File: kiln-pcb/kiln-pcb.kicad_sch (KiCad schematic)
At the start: 12 parts, among them J1 TFT, J2 TEMP, J3 ROTARY, J4 Relay, U1 WeMos_D1_mini

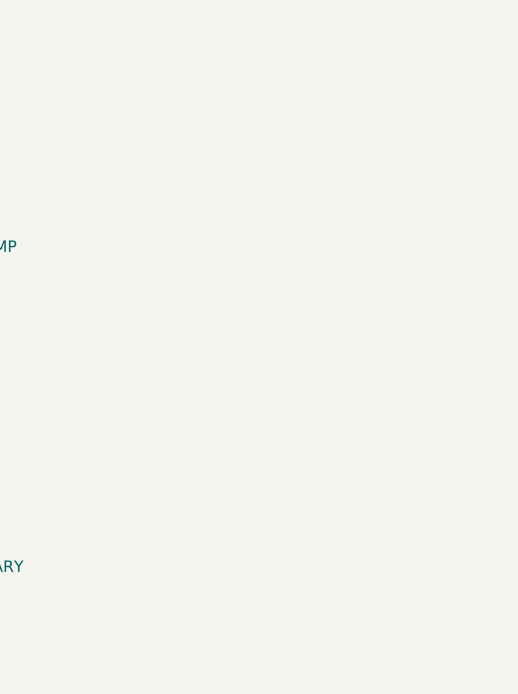
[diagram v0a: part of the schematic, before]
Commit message: Added simple PID for relay
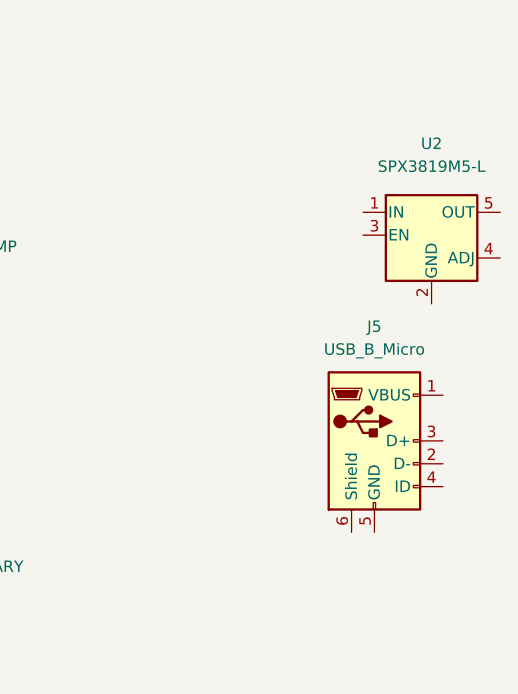
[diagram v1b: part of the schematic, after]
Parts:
- added J5: USB_B_Micro, symbol Connector:USB_B_Micro
- added U2: SPX3819M5-L, Package_TO_SOT_SMD:SOT-23-5, symbol Regulator_Linear:SPX3819M5-L
- H1, H2, H3, H4: footprint MountingHole:MountingHole_3.2mm_M3 -> MountingHole:MountingHole_3.2mm_M3_Pad_Via
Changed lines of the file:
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@@
       (effects (font (size 1.27 1.27)) (justify left))
     )
-    (property "Footprint" "MountingHole:MountingHole_3.2mm_M3" (id 2) (at 134.62 125.73 0)
+    (property "Footprint" "MountingHole:MountingHole_3.2mm_M3_Pad_Via" (id 2) (at 134.62 125.73 0)
       (effects (font (size 1.27 1.27)) hide)
     )
@@
     (pin "1")
   )
+  (symbol (lib_id "Regulator_Linear:SPX3819M5-L") (at 205.74 44.45 0) (unit 1)
+    (in_bom yes) (on_board yes) (fields_autoplaced)
+    (property "Reference" "U2" (id 0) (at 205.74 34.29 0))
+    (property "Value" "SPX3819M5-L" (id 1) (at 205.74 36.83 0))
+    (property "Footprint" "Package_TO_SOT_SMD:SOT-23-5" (id 2) (at 205.74 36.195 0)
+      (effects (font (size 1.27 1.27)) hide)
+    )
+    (property "Datasheet" "https://www.exar.com/content/document.ashx?id=22106&languageid=1033&type=Datasheet&partnumber=SPX3819&filename=SPX3819.pdf&part=SPX3819" (id 3) (at 205.74 44.45 0)
+      (effects (font (size 1.27 1.27)) hide)
+    )
+    (pin "1")
+    (pin "2")
+    (pin "3")
+    (pin "4")
+    (pin "5")
+  )
   (symbol (lib_id "Connector:TestPoint") (at 63.5 99.06 270) (unit 1)
     (in_bom yes) (on_board yes) (fields_autoplaced)
@@
       (effects (font (size 1.27 1.27)) (justify left))
     )
-    (property "Footprint" "MountingHole:MountingHole_3.2mm_M3" (id 2) (at 124.46 115.57 0)
+    (property "Footprint" "MountingHole:MountingHole_3.2mm_M3_Pad_Via" (id 2) (at 124.46 115.57 0)
       (effects (font (size 1.27 1.27)) hide)
     )
@@
       (effects (font (size 1.27 1.27)) (justify left))
     )
-    (property "Footprint" "MountingHole:MountingHole_3.2mm_M3" (id 2) (at 124.46 125.73 0)
+    (property "Footprint" "MountingHole:MountingHole_3.2mm_M3_Pad_Via" (id 2) (at 124.46 125.73 0)
       (effects (font (size 1.27 1.27)) hide)
     )
@@
       (effects (font (size 1.27 1.27)) (justify left))
     )
-    (property "Footprint" "MountingHole:MountingHole_3.2mm_M3" (id 2) (at 133.35 115.57 0)
+    (property "Footprint" "MountingHole:MountingHole_3.2mm_M3_Pad_Via" (id 2) (at 133.35 115.57 0)
       (effects (font (size 1.27 1.27)) hide)
     )
@@
     (pin "4")
     (pin "5")
+  )
+  (symbol (lib_id "Connector:USB_B_Micro") (at 199.39 67.31 0) (unit 1)
+    (in_bom yes) (on_board yes) (fields_autoplaced)
+    (property "Reference" "J5" (id 0) (at 199.39 54.61 0))
+    (property "Value" "USB_B_Micro" (id 1) (at 199.39 57.15 0))
+    (property "Footprint" "" (id 2) (at 203.2 68.58 0)
+      (effects (font (size 1.27 1.27)) hide)
+    )
+    (property "Datasheet" "~" (id 3) (at 203.2 68.58 0)
+      (effects (font (size 1.27 1.27)) hide)
+    )
+    (pin "1")
+    (pin "2")
+    (pin "3")
+    (pin "4")
+    (pin "5")
+    (pin "6")
   )
   (sheet_instances
@@
     )
     (path "/aa1c6f47-cbd4-4cbd-8265-e5ac08b7ffc8"
-      (reference "H1") (unit 1) (value "MountingHole") (footprint "MountingHole:MountingHole_3.2mm_M3")
+      (reference "H1") (unit 1) (value "MountingHole") (footprint "MountingHole:MountingHole_3.2mm_M3_Pad_Via")
     )
     (path "/b2944857-047d-4655-a00b-49e658220448"
-      (reference "H2") (unit 1) (value "MountingHole") (footprint "MountingHole:MountingHole_3.2mm_M3")
+      (reference "H2") (unit 1) (value "MountingHole") (footprint "MountingHole:MountingHole_3.2mm_M3_Pad_Via")
     )
     (path "/d068a394-7054-45f9-ac53-014bf75c7213"
-      (reference "H3") (unit 1) (value "MountingHole") (footprint "MountingHole:MountingHole_3.2mm_M3")
+      (reference "H3") (unit 1) (value "MountingHole") (footprint "MountingHole:MountingHole_3.2mm_M3_Pad_Via")
     )
     (path "/25f1074a-6ae7-40ed-8106-5e5622cabe99"
-      (reference "H4") (unit 1) (value "MountingHole") (footprint "MountingHole:MountingHole_3.2mm_M3")
+      (reference "H4") (unit 1) (value "MountingHole") (footprint "MountingHole:MountingHole_3.2mm_M3_Pad_Via")
     )
     (path "/5fada503-749c-4ab1-b15f-4f7e43d6c0e6"
@@
       (reference "J4") (unit 1) (value "Relay") (footprint "Connector_PinHeader_2.54mm:PinHeader_1x03_P2.54mm_Vertical")
     )
+    (path "/e37d567c-6591-4d58-92e7-b351e9f98d1e"
+      (reference "J5") (unit 1) (value "USB_B_Micro") (footprint "Connector_USB:USB_Micro-B_Molex-105017-0001")
+    )
     (path "/4bb6aa50-20a8-40c0-9694-aa4503d2e061"
       (reference "TP1") (unit 1) (value "5V test") (footprint "TestPoint:TestPoint_Pad_D2.0mm")
@@
       (reference "U1") (unit 1) (value "WeMos_D1_mini") (footprint "Module:WEMOS_D1_mini_light")
     )
-  )
+    (path "/87e2c0d2-6681-45e0-8731-ac0b4ab5761c"
+      (reference "U2") (unit 1) (value "SPX3819M5-L") (footprint "Package_TO_SOT_SMD:SOT-23-5")
+    )
+  )

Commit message: PCB v1.1
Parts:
- removed J5: USB_B_Micro, symbol Connector:USB_B_Micro
- removed U2: SPX3819M5-L, Package_TO_SOT_SMD:SOT-23-5, symbol Regulator_Linear:SPX3819M5-L
- added J5, J6: Relay, Connector_PinHeader_2.54mm:PinHeader_1x03_P2.54mm_Vertical, symbol Connector:Conn_01x03_Male
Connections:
- net CS_T: now also U1.16 (TX); no longer J1.2 (Pin_2), U1.7 (CS/D8)
- net GND: now also J5.2 (Pin_2), J6.2 (Pin_2)
- net Sig_relay: now also J5.1 (Pin_1), J6.1 (Pin_1)
- net Vcc_relay: now also J5.3 (Pin_3), J6.3 (Pin_3)
- new net CS_TFT: J1.2 (Pin_2), U1.7 (CS/D8)
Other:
- moved on the sheet: J1, J2, J3, J4

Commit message: Basic README update
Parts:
- removed H1, H2, H3, H4: MountingHole, MountingHole:MountingHole_3.2mm_M3_Pad_Via, symbol Mechanical:MountingHole
- TP1: value 5V test -> 5V
- TP2: value GND test -> GND
- TP3: value Relay signal -> Relay
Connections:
- net Vcc_relay renamed 3V3
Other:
- moved on the sheet: J1, J2, J3, J4, J5, J6, TP1, TP2, TP3, U1

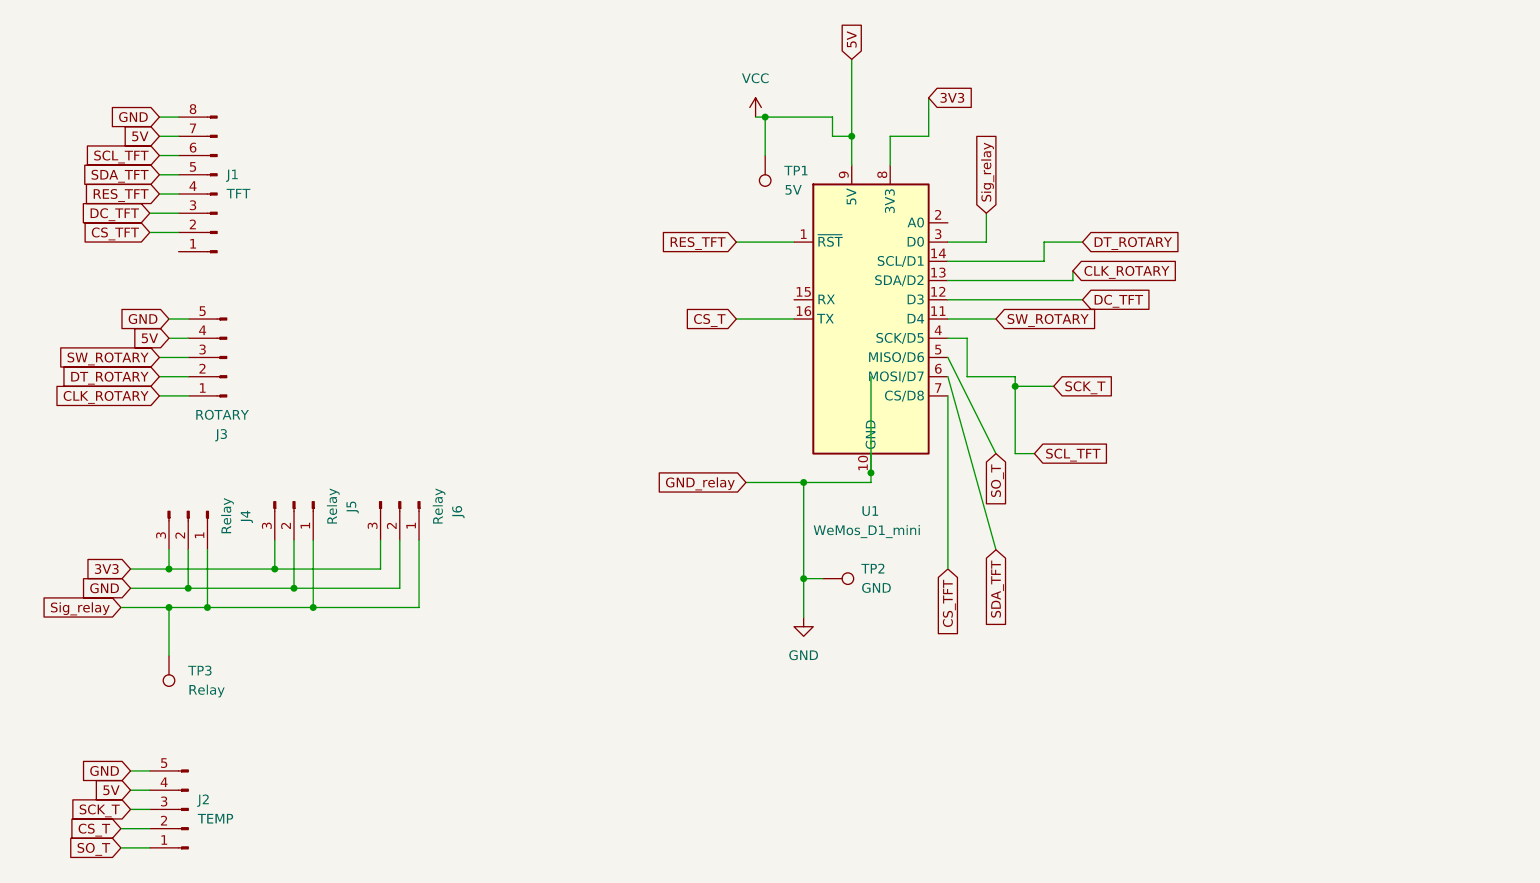
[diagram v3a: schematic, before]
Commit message: Added magnetic switch interrupt
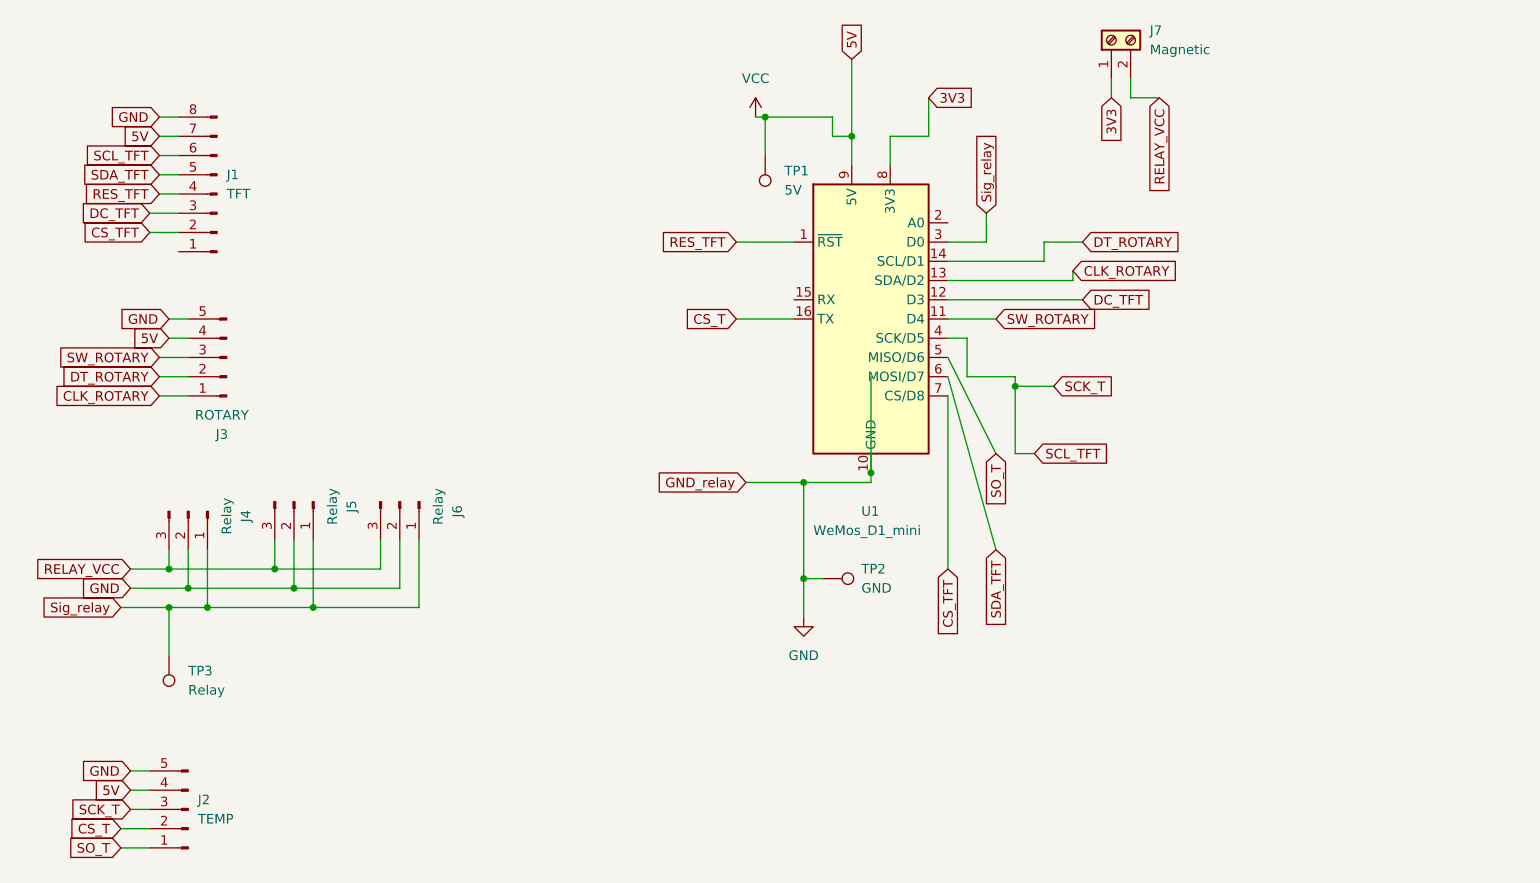
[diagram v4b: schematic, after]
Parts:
- added J7: Magnetic, TerminalBlock:TerminalBlock_bornier-2_P5.08mm, symbol Connector:Screw_Terminal_01x02
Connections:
- net 3V3: now also J7.1 (Pin_1); no longer J4.3 (Pin_3), J5.3 (Pin_3), J6.3 (Pin_3)
- new net RELAY_VCC: J4.3 (Pin_3), J5.3 (Pin_3), J6.3 (Pin_3), J7.2 (Pin_2)
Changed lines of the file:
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@@
+    (stroke (width 0) (type default) (color 0 0 0 0))
+  )
+  (wire (pts (xy 161.29 26.67) (xy 165.1 26.67))
     (stroke (width 0) (type default) (color 0 0 0 0))
   )
@@
     (stroke (width 0) (type default) (color 0 0 0 0))
   )
+  (wire (pts (xy 158.75 24.13) (xy 158.75 26.67))
+    (stroke (width 0) (type default) (color 0 0 0 0))
+  )
   (wire (pts (xy 50.8 85.09) (xy 50.8 91.44))
     (stroke (width 0) (type default) (color 0 0 0 0))
@@
     (stroke (width 0) (type default) (color 0 0 0 0))
   )
+  (wire (pts (xy 161.29 24.13) (xy 161.29 26.67))
+    (stroke (width 0) (type default) (color 0 0 0 0))
+  )
   (wire (pts (xy 137.16 66.04) (xy 137.16 88.9))
     (stroke (width 0) (type default) (color 0 0 0 0))
@@
     (stroke (width 0) (type default) (color 0 0 0 0))
   )
+  (global_label "3V3" (shape input) (at 158.75 26.67 270) (fields_autoplaced)
+    (effects (font (size 1.27 1.27)) (justify right))
+    (property "Intersheet References" "${INTERSHEET_REFS}" (id 0) (at 158.6706 32.5907 90)
+      (effects (font (size 1.27 1.27)) (justify right) hide)
+    )
+  )
   (global_label "5V" (shape input) (at 124.46 21.59 90) (fields_autoplaced)
     (effects (font (size 1.27 1.27)) (justify left))
@@
     )
   )
+  (global_label "RELAY_VCC" (shape input) (at 165.1 26.67 270) (fields_autoplaced)
+    (effects (font (size 1.27 1.27)) (justify right))
+    (property "Intersheet References" "${INTERSHEET_REFS}" (id 0) (at 165.0206 39.3036 90)
+      (effects (font (size 1.27 1.27)) (justify right) hide)
+    )
+  )
   (global_label "DT_ROTARY" (shape input) (at 154.94 45.72 0) (fields_autoplaced)
     (effects (font (size 1.27 1.27)) (justify left))
@@
     )
   )
-  (global_label "3V3" (shape input) (at 29.21 88.9 180) (fields_autoplaced)
-    (effects (font (size 1.27 1.27)) (justify right))
-    (property "Intersheet References" "${INTERSHEET_REFS}" (id 0) (at 23.2893 88.8206 0)
+  (global_label "RELAY_VCC" (shape input) (at 29.21 88.9 180) (fields_autoplaced)
+    (effects (font (size 1.27 1.27)) (justify right))
+    (property "Intersheet References" "${INTERSHEET_REFS}" (id 0) (at 16.5764 88.8206 0)
       (effects (font (size 1.27 1.27)) (justify right) hide)
     )
@@
     )
     (pin "1")
+  )
+  (symbol (lib_id "Connector:Screw_Terminal_01x02") (at 158.75 19.05 90) (unit 1)
+    (in_bom yes) (on_board yes) (fields_autoplaced)
+    (property "Reference" "J7" (id 0) (at 163.83 17.7799 90)
+      (effects (font (size 1.27 1.27)) (justify right))
+    )
+    (property "Value" "Magnetic" (id 1) (at 163.83 20.3199 90)
+      (effects (font (size 1.27 1.27)) (justify right))
+    )
+    (property "Footprint" "TerminalBlock:TerminalBlock_bornier-2_P5.08mm" (id 2) (at 158.75 19.05 0)
+      (effects (font (size 1.27 1.27)) hide)
+    )
+    (property "Datasheet" "~" (id 3) (at 158.75 19.05 0)
+      (effects (font (size 1.27 1.27)) hide)
+    )
+    (pin "1")
+    (pin "2")
   )
   (symbol (lib_id "MCU_Module:WeMos_D1_mini") (at 127 55.88 0) (unit 1)
@@
       (reference "J6") (unit 1) (value "Relay") (footprint "Connector_PinHeader_2.54mm:PinHeader_1x03_P2.54mm_Vertical")
     )
+    (path "/4bf158da-c0cd-4dd4-ac74-cfc531d89522"
+      (reference "J7") (unit 1) (value "Magnetic") (footprint "TerminalBlock:TerminalBlock_bornier-2_P5.08mm")
+    )
     (path "/4bb6aa50-20a8-40c0-9694-aa4503d2e061"
